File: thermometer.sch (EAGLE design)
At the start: 17 parts, among them IC1 MPQ3906, IC2 MPQ3904, IC4 CD4066BE, IC5 LM311N, IC6 LM324N

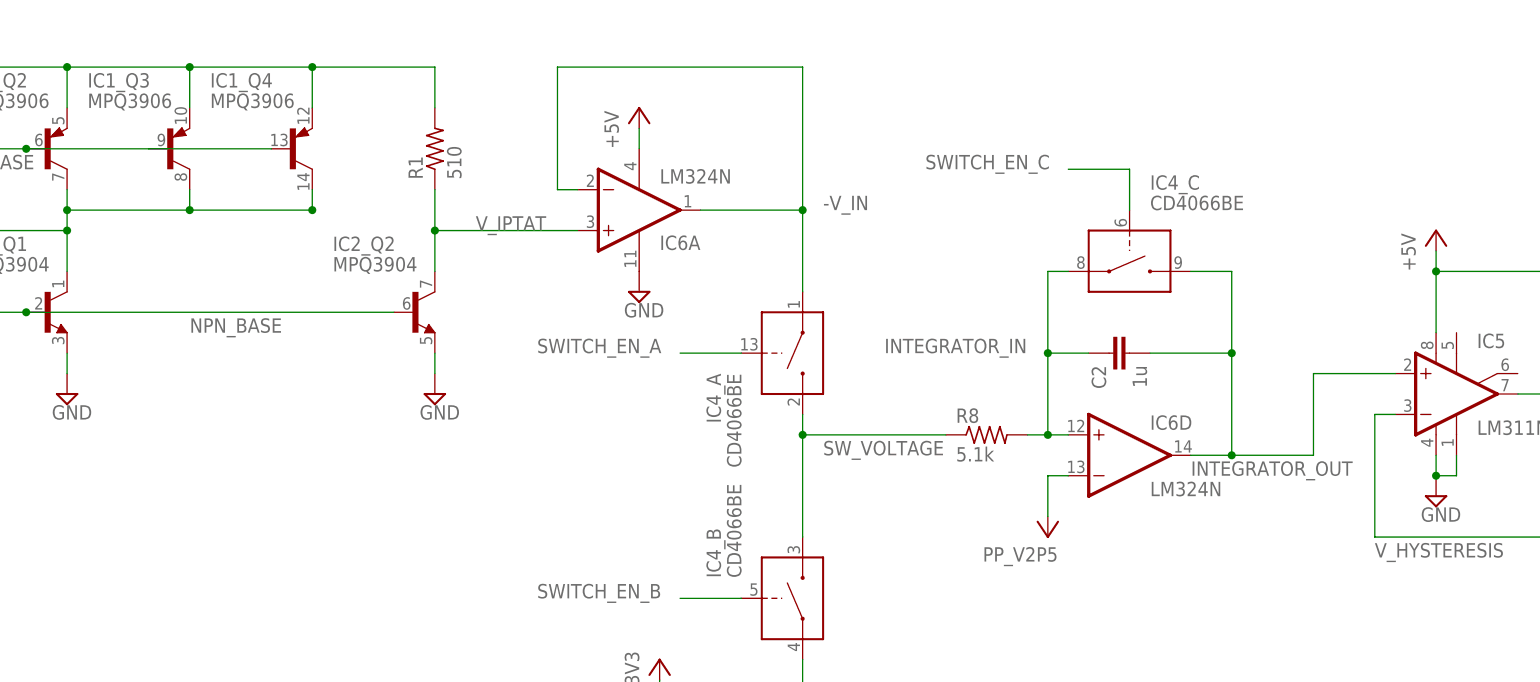
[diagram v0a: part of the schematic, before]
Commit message: fixed in+ and in- pins of op amps and comparator
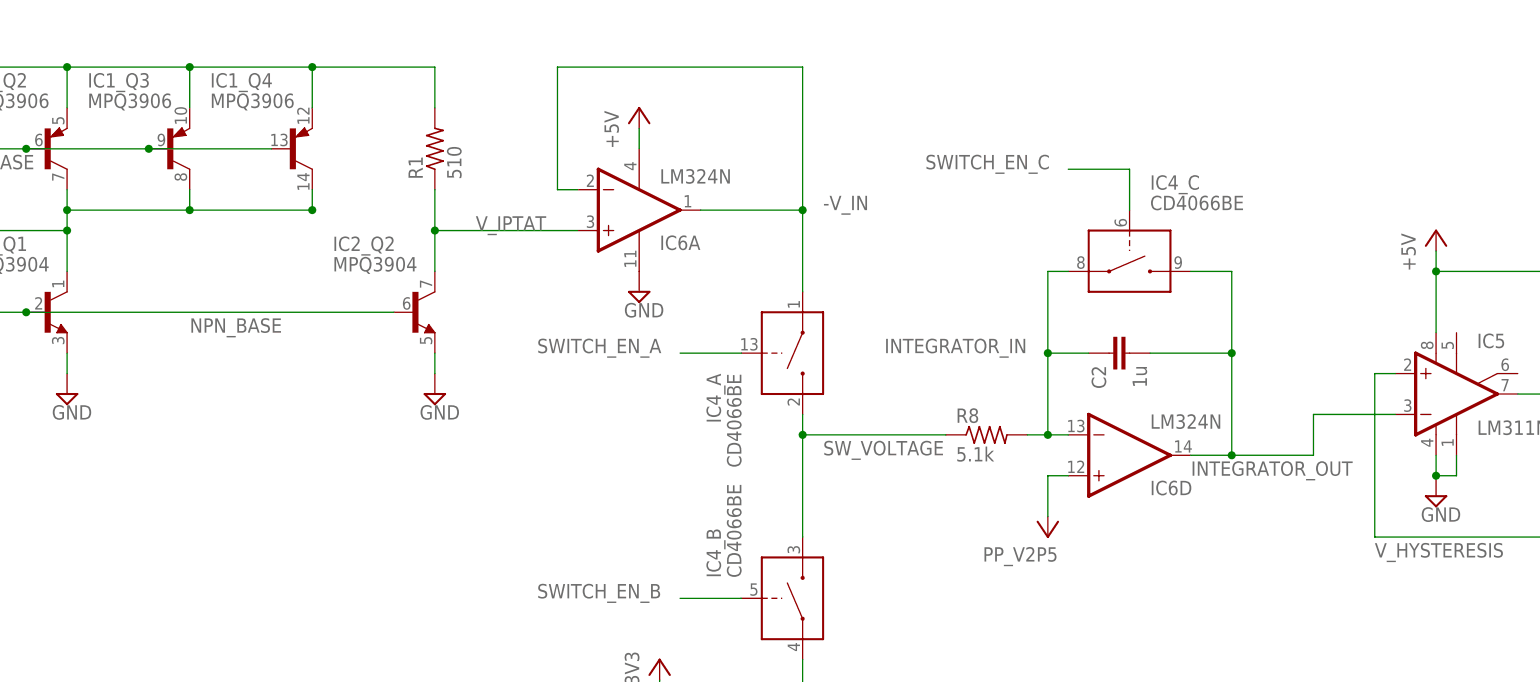
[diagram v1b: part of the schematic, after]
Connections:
- net INTEGRATOR_IN: now also IC6D.-IN; no longer IC6D.+IN
- net INTEGRATOR_OUT: now also IC5.-IN; no longer IC5.+IN
- net V+: now also IC6D.+IN; no longer IC6D.-IN
- net V_HYSTERESIS: now also IC5.+IN; no longer IC5.-IN
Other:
- moved on the sheet: IC6D
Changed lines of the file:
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@@
 <setting verticaltext="up"/>
 </settings>
-<grid distance="0.1" unitdist="inch" unit="inch" style="lines" multiple="1" display="yes" altdistance="0.01" altunitdist="inch" altunit="inch"/>
+<grid distance="0.1" unitdist="inch" unit="inch" style="lines" multiple="1" display="no" altdistance="0.01" altunitdist="inch" altunit="inch"/>
 <layers>
-<layer number="1" name="Top" color="4" fill="1" visible="yes" active="no"/>
-<layer number="16" name="Bottom" color="1" fill="1" visible="yes" active="no"/>
-<layer number="17" name="Pads" color="2" fill="1" visible="yes" active="no"/>
-<layer number="18" name="Vias" color="2" fill="1" visible="yes" active="no"/>
-<layer number="19" name="Unrouted" color="6" fill="1" visible="yes" active="no"/>
-<layer number="20" name="Dimension" color="15" fill="1" visible="yes" active="no"/>
-<layer number="21" name="tPlace" color="7" fill="1" visible="yes" active="no"/>
-<layer number="22" name="bPlace" color="7" fill="1" visible="yes" active="no"/>
-<layer number="23" name="tOrigins" color="15" fill="1" visible="yes" active="no"/>
-<layer number="24" name="bOrigins" color="15" fill="1" visible="yes" active="no"/>
-<layer number="25" name="tNames" color="7" fill="1" visible="yes" active="no"/>
-<layer number="26" name="bNames" color="7" fill="1" visible="yes" active="no"/>
-<layer number="27" name="tValues" color="7" fill="1" visible="yes" active="no"/>
-<layer number="28" name="bValues" color="7" fill="1" visible="yes" active="no"/>
+<layer number="1" name="Top" color="4" fill="1" visible="no" active="no"/>
+<layer number="16" name="Bottom" color="1" fill="1" visible="no" active="no"/>
+<layer number="17" name="Pads" color="2" fill="1" visible="no" active="no"/>
+<layer number="18" name="Vias" color="2" fill="1" visible="no" active="no"/>
+<layer number="19" name="Unrouted" color="6" fill="1" visible="no" active="no"/>
+<layer number="20" name="Dimension" color="15" fill="1" visible="no" active="no"/>
+<layer number="21" name="tPlace" color="7" fill="1" visible="no" active="no"/>
+<layer number="22" name="bPlace" color="7" fill="1" visible="no" active="no"/>
+<layer number="23" name="tOrigins" color="15" fill="1" visible="no" active="no"/>
+<layer number="24" name="bOrigins" color="15" fill="1" visible="no" active="no"/>
+<layer number="25" name="tNames" color="7" fill="1" visible="no" active="no"/>
+<layer number="26" name="bNames" color="7" fill="1" visible="no" active="no"/>
+<layer number="27" name="tValues" color="7" fill="1" visible="no" active="no"/>
+<layer number="28" name="bValues" color="7" fill="1" visible="no" active="no"/>
 <layer number="29" name="tStop" color="7" fill="3" visible="no" active="no"/>
 <layer number="30" name="bStop" color="7" fill="6" visible="no" active="no"/>
@@
 <layer number="35" name="tGlue" color="7" fill="4" visible="no" active="no"/>
 <layer number="36" name="bGlue" color="7" fill="5" visible="no" active="no"/>
-<layer number="37" name="tTest" color="7" fill="1" visible="yes" active="no"/>
-<layer number="38" name="bTest" color="7" fill="1" visible="yes" active="no"/>
+<layer number="37" name="tTest" color="7" fill="1" visible="no" active="no"/>
+<layer number="38" name="bTest" color="7" fill="1" visible="no" active="no"/>
 <layer number="39" name="tKeepout" color="4" fill="11" visible="no" active="no"/>
 <layer number="40" name="bKeepout" color="1" fill="11" visible="no" active="no"/>
@@
 <layer number="44" name="Drills" color="7" fill="1" visible="no" active="no"/>
 <layer number="45" name="Holes" color="7" fill="1" visible="no" active="no"/>
-<layer number="46" name="Milling" color="3" fill="1" visible="yes" active="no"/>
-<layer number="47" name="Measures" color="7" fill="1" visible="yes" active="no"/>
-<layer number="48" name="Document" color="7" fill="1" visible="yes" active="no"/>
-<layer number="49" name="Reference" color="7" fill="1" visible="yes" active="no"/>
-<layer number="50" name="dxf" color="7" fill="1" visible="yes" active="no"/>
-<layer number="51" name="tDocu" color="7" fill="1" visible="yes" active="no"/>
-<layer number="52" name="bDocu" color="7" fill="1" visible="yes" active="no"/>
-<layer number="53" name="tPadExt" color="7" fill="1" visible="yes" active="no"/>
-<layer number="54" name="bPadExt" color="1" fill="1" visible="yes" active="no"/>
-<layer number="56" name="wert" color="7" fill="1" visible="yes" active="no"/>
+<layer number="46" name="Milling" color="3" fill="1" visible="no" active="no"/>
+<layer number="47" name="Measures" color="7" fill="1" visible="no" active="no"/>
+<layer number="48" name="Document" color="7" fill="1" visible="no" active="no"/>
+<layer number="49" name="Reference" color="7" fill="1" visible="no" active="no"/>
+<layer number="50" name="dxf" color="7" fill="1" visible="no" active="no"/>
+<layer number="51" name="tDocu" color="7" fill="1" visible="no" active="no"/>
+<layer number="52" name="bDocu" color="7" fill="1" visible="no" active="no"/>
+<layer number="53" name="tPadExt" color="7" fill="1" visible="no" active="no"/>
+<layer number="54" name="bPadExt" color="1" fill="1" visible="no" active="no"/>
+<layer number="56" name="wert" color="7" fill="1" visible="no" active="no"/>
 <layer number="90" name="Modules" color="5" fill="1" visible="yes" active="yes"/>
 <layer number="91" name="Nets" color="2" fill="1" visible="yes" active="yes"/>
@@
 <instance part="SUPPLY7" gate="GND" x="208.28" y="147.32"/>
 <instance part="SUPPLY8" gate="GND" x="154.94" y="139.7"/>
-<instance part="IC6" gate="D" x="182.88" y="38.1"/>
+<instance part="IC6" gate="D" x="182.88" y="38.1" rot="MR180"/>
 <instance part="IC6" gate="P" x="121.92" y="68.58"/>
 <instance part="PP_V5P0_ARDUINO4" gate="1" x="121.92" y="81.28"/>
@@
 </segment>
 <segment>
-<wire x1="175.26" y1="35.56" x2="172.72" y2="35.56" width="0.1524" layer="91"/>
 <pinref part="PP_V2P2" gate="1" pin="V+"/>
 <wire x1="172.72" y1="35.56" x2="172.72" y2="30.48" width="0.1524" layer="91"/>
-<pinref part="IC6" gate="D" pin="-IN"/>
+<pinref part="IC6" gate="D" pin="+IN"/>
+<wire x1="172.72" y1="35.56" x2="175.26" y2="35.56" width="0.1524" layer="91"/>
 </segment>
 </net>
@@
 <label x="35.56" y="73.66" size="1.778" layer="95"/>
 <junction x="45.72" y="76.2"/>
+<junction x="60.96" y="76.2"/>
 </segment>
 </net>
@@
 <pinref part="R6" gate="G$1" pin="1"/>
 <wire x1="238.76" y1="25.4" x2="238.76" y2="27.94" width="0.1524" layer="91"/>
-<pinref part="IC5" gate="A" pin="-IN"/>
 <wire x1="238.76" y1="27.94" x2="238.76" y2="33.02" width="0.1524" layer="91"/>
-<wire x1="215.9" y1="43.18" x2="213.36" y2="43.18" width="0.1524" layer="91"/>
-<wire x1="213.36" y1="43.18" x2="213.36" y2="27.94" width="0.1524" layer="91"/>
 <wire x1="213.36" y1="27.94" x2="238.76" y2="27.94" width="0.1524" layer="91"/>
 <junction x="238.76" y="27.94"/>
 <label x="213.36" y="25.4" size="1.778" layer="95"/>
+<wire x1="213.36" y1="27.94" x2="213.36" y2="48.26" width="0.1524" layer="91"/>
+<pinref part="IC5" gate="A" pin="+IN"/>
+<wire x1="213.36" y1="48.26" x2="215.9" y2="48.26" width="0.1524" layer="91"/>
 </segment>
 </net>
@@
 <wire x1="170.18" y1="40.64" x2="172.72" y2="40.64" width="0.1524" layer="91"/>
 <pinref part="C2" gate="G$1" pin="1"/>
-<wire x1="172.72" y1="40.64" x2="175.26" y2="40.64" width="0.1524" layer="91"/>
 <wire x1="177.8" y1="50.8" x2="172.72" y2="50.8" width="0.1524" layer="91"/>
 <wire x1="172.72" y1="50.8" x2="172.72" y2="40.64" width="0.1524" layer="91"/>
@@
 <wire x1="175.26" y1="60.96" x2="172.72" y2="60.96" width="0.1524" layer="91"/>
 <wire x1="172.72" y1="60.96" x2="172.72" y2="50.8" width="0.1524" layer="91"/>
-<junction x="172.72" y="40.64"/>
 <junction x="172.72" y="50.8"/>
 <label x="152.4" y="50.8" size="1.778" layer="95"/>
-<pinref part="IC6" gate="D" pin="+IN"/>
+<pinref part="IC6" gate="D" pin="-IN"/>
+<wire x1="172.72" y1="40.64" x2="175.26" y2="40.64" width="0.1524" layer="91"/>
+<junction x="172.72" y="40.64"/>
 </segment>
 </net>
@@
 <wire x1="185.42" y1="50.8" x2="195.58" y2="50.8" width="0.1524" layer="91"/>
 <wire x1="195.58" y1="50.8" x2="195.58" y2="38.1" width="0.1524" layer="91"/>
-<wire x1="195.58" y1="38.1" x2="190.5" y2="38.1" width="0.1524" layer="91"/>
 <wire x1="195.58" y1="50.8" x2="195.58" y2="60.96" width="0.1524" layer="91"/>
 <pinref part="IC4" gate="_C" pin="IN/OUT2"/>
 <wire x1="195.58" y1="60.96" x2="190.5" y2="60.96" width="0.1524" layer="91"/>
 <wire x1="195.58" y1="38.1" x2="205.74" y2="38.1" width="0.1524" layer="91"/>
-<wire x1="205.74" y1="38.1" x2="205.74" y2="48.26" width="0.1524" layer="91"/>
-<pinref part="IC5" gate="A" pin="+IN"/>
-<wire x1="205.74" y1="48.26" x2="215.9" y2="48.26" width="0.1524" layer="91"/>
 <junction x="195.58" y="50.8"/>
-<junction x="195.58" y="38.1"/>
 <label x="190.5" y="35.56" size="1.778" layer="95"/>
 <pinref part="IC6" gate="D" pin="OUT"/>
-</segment>
-</net>
+<wire x1="190.5" y1="38.1" x2="195.58" y2="38.1" width="0.1524" layer="91"/>
+<junction x="195.58" y="38.1"/>
+<wire x1="205.74" y1="38.1" x2="205.74" y2="43.18" width="0.1524" layer="91"/>
+<pinref part="IC5" gate="A" pin="-IN"/>
+<wire x1="205.74" y1="43.18" x2="215.9" y2="43.18" width="0.1524" layer="91"/>
+</segment>
+</net>

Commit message: fixed labelling
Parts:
- IC6: value LM324N -> LM6134
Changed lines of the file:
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@@
 <part name="R7" library="rcl" deviceset="R-US_" device="0207/10" value="680"/>
 <part name="PP_V2P3" library="supply2" deviceset="V+" device="" value="PP_V2P5"/>
-<part name="IC6" library="linear" deviceset="LM324" device="N"/>
+<part name="IC6" library="linear" deviceset="LM324" device="N" value="LM6134"/>
 <part name="C2" library="rcl" deviceset="C-EU" device="050-035X075" value="1u"/>
 <part name="R8" library="rcl" deviceset="R-US_" device="0207/10" value="5.1k"/>
